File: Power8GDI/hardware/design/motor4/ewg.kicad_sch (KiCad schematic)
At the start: 16 parts, among them U6050 TLE9201SG, U6051 SN74LVC1G32QDBVRQ1

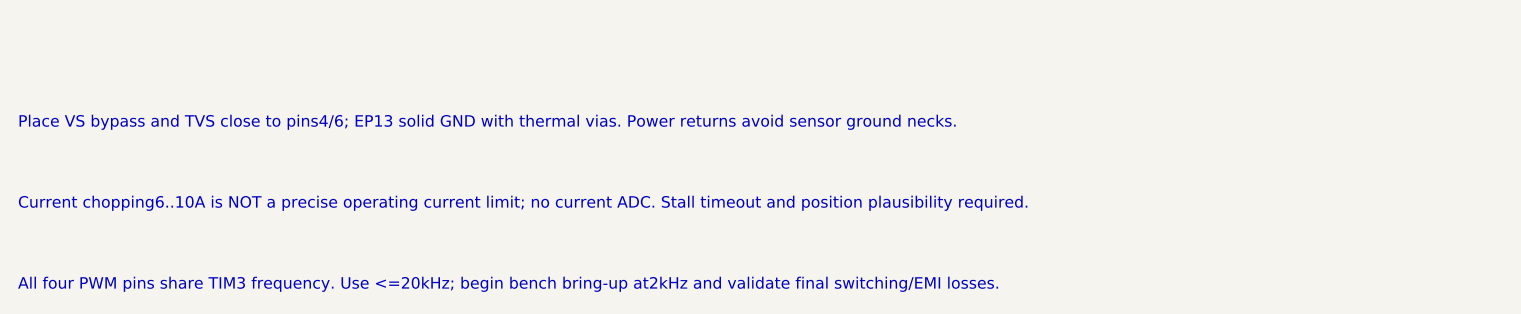
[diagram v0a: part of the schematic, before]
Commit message: Redesign sport target as six DI/PI channels with two motors and one lambda
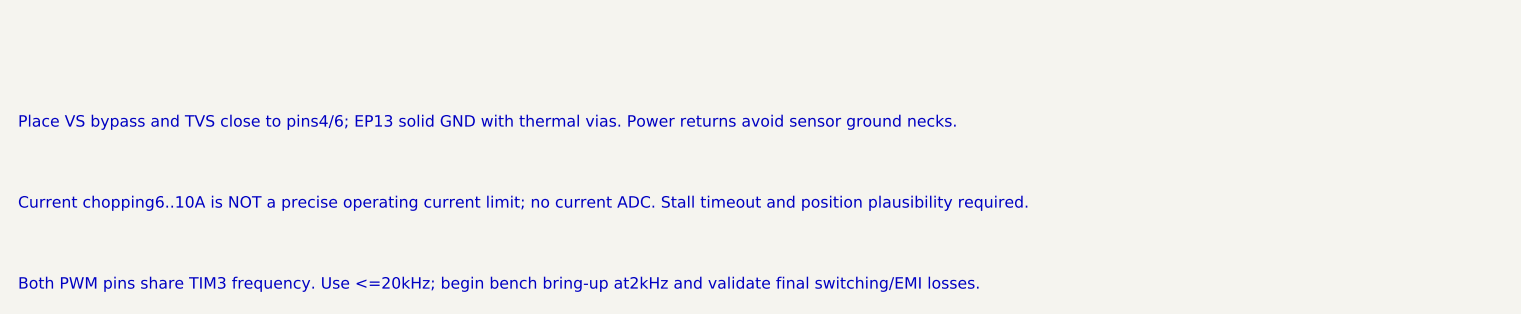
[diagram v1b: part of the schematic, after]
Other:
- note added: "Both PWM pins share TIM3 frequency. Use <=20kHz; begin bench bring-up at2kHz and validate final switching/EMI losses."
- note removed: "All four PWM pins share TIM3 frequency. Use <=20kHz; begin bench bring-up at2kHz and validate final switching/EMI losses."
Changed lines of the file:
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@@
 (text "Place VS bypass and TVS close to pins4/6; EP13 solid GND with thermal vias. Power returns avoid sensor ground necks." (at 20 355 0) (effects (font (size 1.27 1.27)) (justify left top)))
 (text "Current chopping6..10A is NOT a precise operating current limit; no current ADC. Stall timeout and position plausibility required." (at 20 364 0) (effects (font (size 1.27 1.27)) (justify left top)))
-(text "All four PWM pins share TIM3 frequency. Use <=20kHz; begin bench bring-up at2kHz and validate final switching/EMI losses." (at 20 373 0) (effects (font (size 1.27 1.27)) (justify left top)))
+(text "Both PWM pins share TIM3 frequency. Use <=20kHz; begin bench bring-up at2kHz and validate final switching/EMI losses." (at 20 373 0) (effects (font (size 1.27 1.27)) (justify left top)))
 (sheet_instances (path "/" (page "1"))))

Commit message: Review B58 injector power stage and bind selected GDI6 BOM
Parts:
- C6050, C6051, C6052: Hardware_Qualification (none) -> BOARD_QUALIFICATION_PENDING; MPN (none) -> C0805C104K1RACTU; Manufacturer (none) -> KEMET; Procurement_Status (none) -> SELECTED_CATALOG_ITEM; Purchase_Released (none) -> false; Selection_Gaps (none) -> []; Selection_ID (none) -> SEL-50b208aec5b1; Selection_Ratings (none) -> {"capacitance_pf": 100000, "dielectric": "X7R", "rated_volt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; Selection_Source_URLs (none) -> https://www.mouser.com/datasheet/3/72/1/C0805C104K1RACTU.pdf
- C6053: Hardware_Qualification (none) -> BOARD_QUALIFICATION_PENDING; MPN (none) -> C1206C105K5RACTU; Manufacturer (none) -> KEMET; Procurement_Status (none) -> SELECTED_CATALOG_ITEM; Purchase_Released (none) -> false; Selection_Gaps (none) -> []; Selection_ID (none) -> SEL-c5dbcfe81b07; Selection_Ratings (none) -> {"capacitance_pf": 1000000, "dc_bias_qualification": "PENDI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; Selection_Source_URLs (none) -> https://www.digikey.com/en/products/detail/kemet/C1206C105K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
- C6054: Hardware_Qualification (none) -> RIPPLE_AND_THERMAL_REVIEW_REQUIRED; MPN (none) -> EEH-ZE1H101P; Manufacturer (none) -> Panasonic Industry; Procurement_Status (none) -> SELECTED_CONDITIONAL; Purchase_Released (none) -> false; Selection_Gaps (none) -> ["EWG/DBW current ripple and thermal lifetime must be check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; Selection_ID (none) -> SEL-3f0c236799d0; Selection_Ratings (none) -> {"aec_q200": true, "capacitance_pf": 100000000, "diameter_m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; Selection_Source_URLs (none) -> https://www.digikey.com/en/products/detail/panasonic-indust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
- C6055, C6056: Hardware_Qualification (none) -> BOARD_QUALIFICATION_PENDING; MPN (none) -> C0805C102J1GACTU; Manufacturer (none) -> KEMET; Procurement_Status (none) -> SELECTED_CATALOG_ITEM; Purchase_Released (none) -> false; Selection_Gaps (none) -> []; Selection_ID (none) -> SEL-861be0060b67; Selection_Ratings (none) -> {"capacitance_pf": 1000, "dielectric": "C0G", "rated_voltag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; Selection_Source_URLs (none) -> https://www.digikey.com/en/products/detail/kemet/C0805C102J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
- D6050: Hardware_Qualification (none) -> PINOUT_RATINGS_AND_DELIVERY_SUFFIX_REVIEW_PENDING; MPN (none) -> SMCJ18CA; Manufacturer (none) -> Littelfuse; Procurement_Status (none) -> REFERENCE_MPN_RETAINED; Purchase_Released (none) -> false; Selection_Gaps (none) -> ["Existing schematic MPN retained. Complete circuit rating/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; Selection_ID (none) -> SEL-1d45eeb44703; Selection_Ratings (none) -> {}; Selection_Source_URLs (none) -> https://www.littelfuse.com/products/tvs-diodes/surface-moun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
- R6050, R6051: Hardware_Qualification (none) -> BOARD_QUALIFICATION_PENDING; MPN (none) -> CRCW0603100RFKEA; Manufacturer (none) -> Vishay; Procurement_Status (none) -> SELECTED_FAMILY_CODE; Purchase_Released (none) -> false; Selection_Gaps (none) -> []; Selection_ID (none) -> SEL-319468e4af3f; Selection_Ratings (none) -> {"aec_q200": true, "derating": "Use manufacturer power vers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; Selection_Source_URLs (none) -> https://www.vishay.com/docs/20035/dcrcwe3.pdf
- R6052, R6053, R6054, R6055: Hardware_Qualification (none) -> BOARD_QUALIFICATION_PENDING; MPN (none) -> CRCW060310K0FKEA; Manufacturer (none) -> Vishay; Procurement_Status (none) -> SELECTED_FAMILY_CODE; Purchase_Released (none) -> false; Selection_Gaps (none) -> []; Selection_ID (none) -> SEL-9c0806476875; Selection_Ratings (none) -> {"aec_q200": true, "derating": "Use manufacturer power vers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; Selection_Source_URLs (none) -> https://www.vishay.com/docs/20035/dcrcwe3.pdf
- U6050: Hardware_Qualification (none) -> MOTOR_STALL_AND_THERMAL_REVIEW_REQUIRED; MPN (none) -> TLE9201SGAUMA1; Manufacturer (none) -> Infineon Technologies; Procurement_Status (none) -> SELECTED_CONDITIONAL; Purchase_Released (none) -> false; Selection_Gaps (none) -> ["6A is overcurrent detection minimum/catalog bridge class,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; Selection_ID (none) -> SEL-0b8a0686cb43; Selection_Ratings (none) -> {"manufacturer_package": "PG-DSO-12", "overcurrent_detectio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; Selection_Source_URLs (none) -> https://www.infineon.com/part/TLE9201SG
- U6051: Hardware_Qualification (none) -> PINOUT_RATINGS_AND_DELIVERY_SUFFIX_REVIEW_PENDING; MPN (none) -> SN74LVC1G32QDBVRQ1; Manufacturer (none) -> Texas Instruments; Procurement_Status (none) -> REFERENCE_MPN_RETAINED; Purchase_Released (none) -> false; Selection_Gaps (none) -> ["Existing schematic MPN retained. Complete circuit rating/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; Selection_ID (none) -> SEL-963f679db0b8; Selection_Ratings (none) -> {}; Selection_Source_URLs (none) -> https://www.ti.com/product/SN74LVC1G32-Q1/part-details/SN74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
